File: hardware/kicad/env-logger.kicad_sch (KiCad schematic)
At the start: 8 parts, among them SW1 BUTTON, U1 ESP32-S3-DevKitM-1, U2 BME280 module (0x76), U3 DS3231 module (0x68)

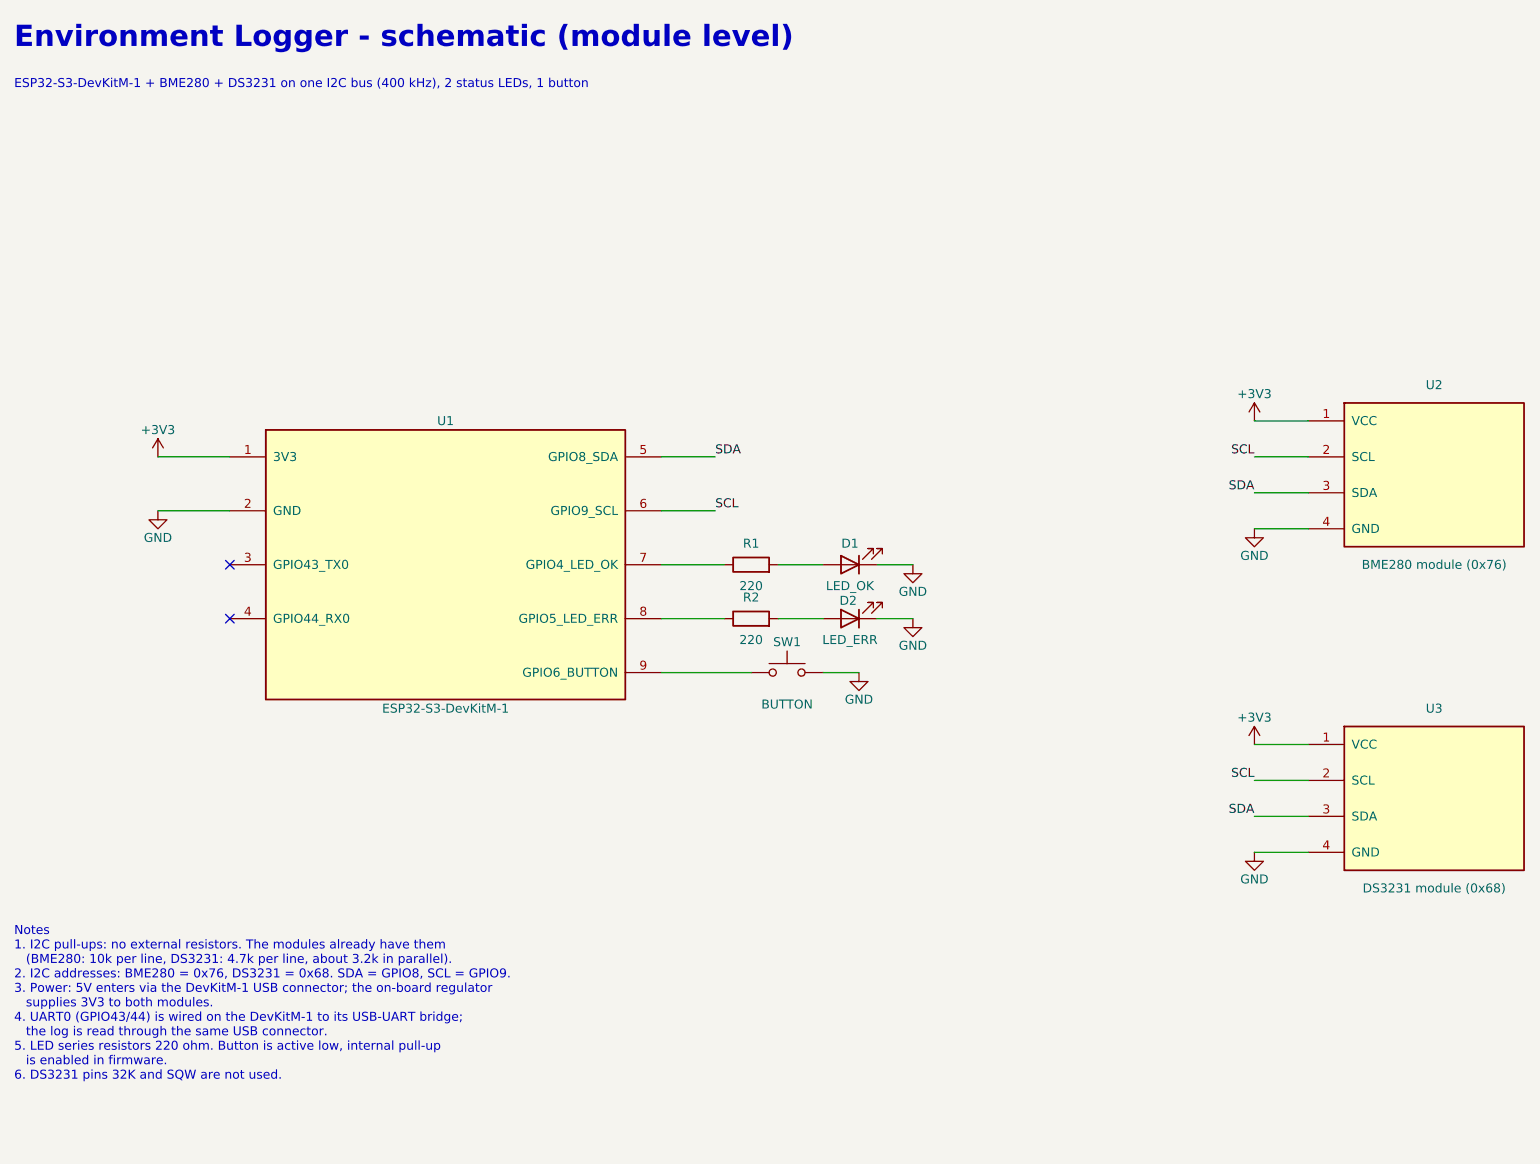
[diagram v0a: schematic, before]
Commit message: Schematic: add unused module pins (BME280 CSB/SDO, DS3231 DS), fix label overlaps
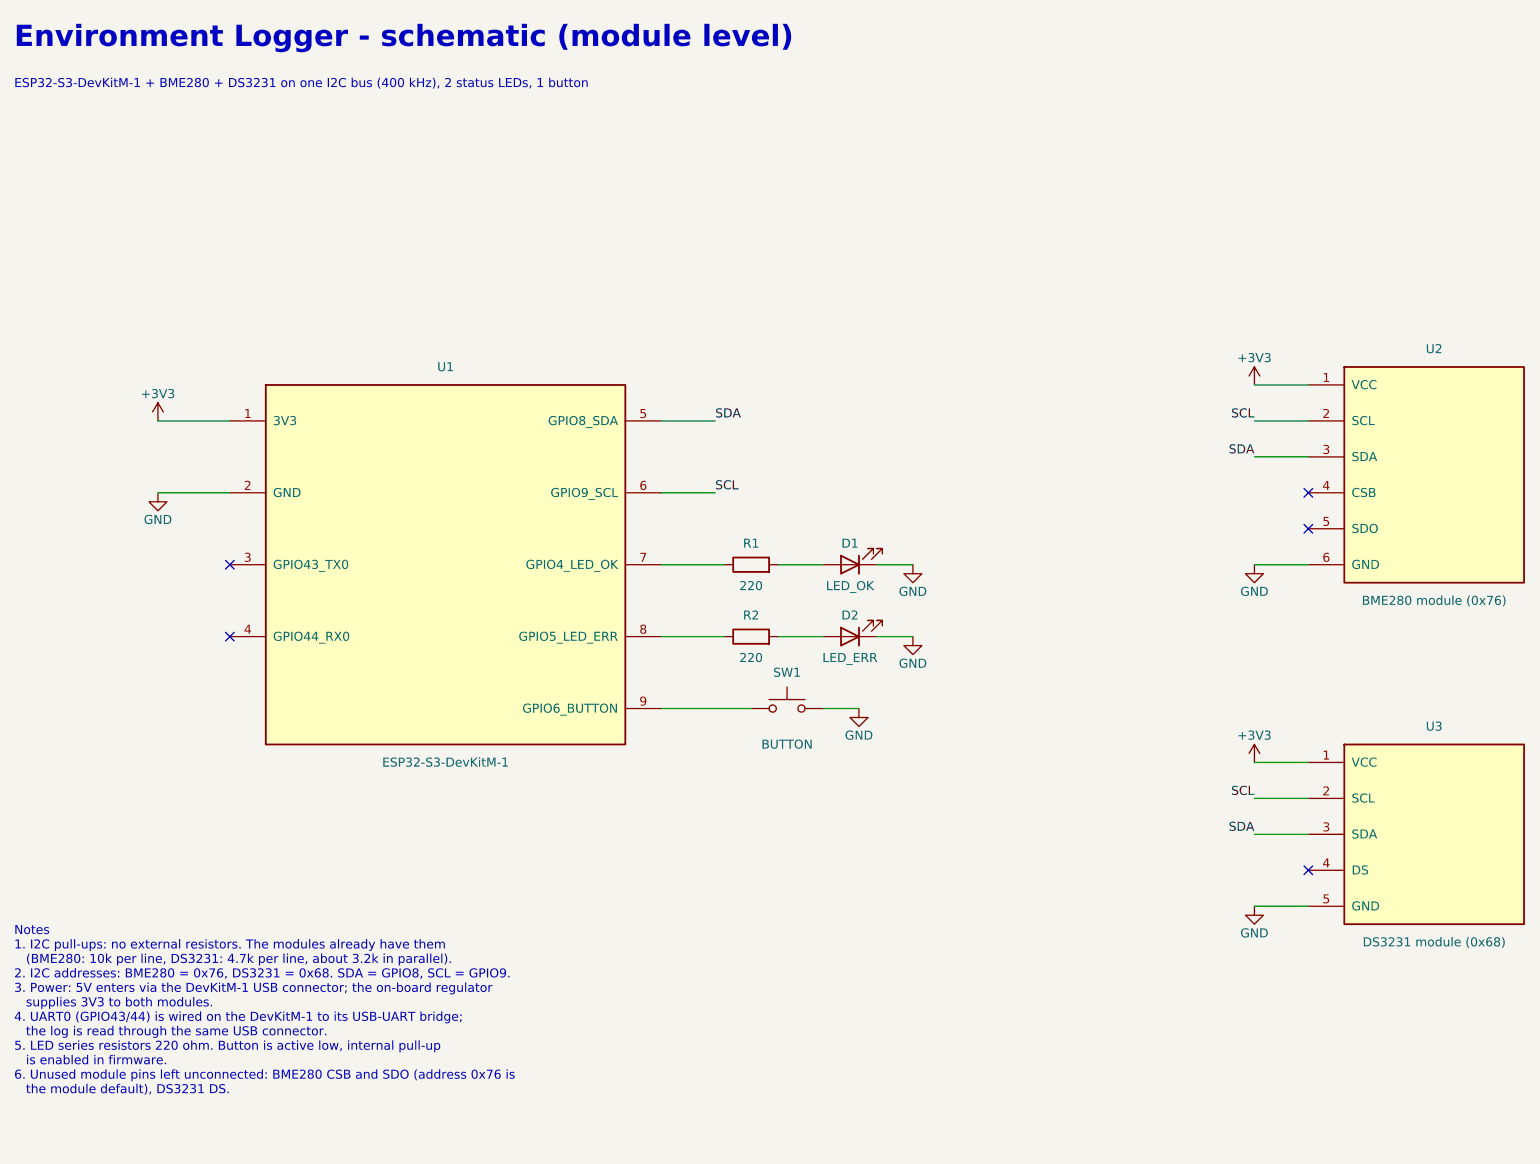
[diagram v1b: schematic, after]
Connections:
- net GND: now also U2.6 (GND), U3.5 (GND); no longer U2.4 (GND), U3.4 (GND)
- no-connect marks 2 -> 5

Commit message: Schematic: the button is a 3-pin module (VCC, GND, OUT) with a pull-down, pressed = high
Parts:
- removed SW1: BUTTON, symbol Switch:SW_Push
- added U4: Button module, symbol env-logger:Button_module
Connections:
- net +3V3: now also U4.1 (VCC)
- net GND: now also U4.3 (GND)
- net BTN: now reaches U1.9 (GPIO6_BUTTON)
- net BTN: now also U4.2 (OUT)
